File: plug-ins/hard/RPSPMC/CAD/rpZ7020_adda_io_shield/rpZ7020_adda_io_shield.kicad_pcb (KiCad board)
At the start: 4 copper layers, 61.3 x 89.9 mm, 24 parts, among them J1 Samtec_ASP-134486-01, J2-FMC-RP1 Conn_02x20, J3-FMC-POWER1 Conn_02x06_Odd_Even, J4-FMC-AUX1 Conn_02x06_Odd_Even

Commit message: fine tune brd
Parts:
- moved MH0 0.51 mm to (122.1, 159.0)
- moved MH1 0.51 mm to (175.7, 159.0)
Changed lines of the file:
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@@
 	(footprint "MountingHole:MountingHole_3.2mm_M3"
 		(layer "F.Cu")
-		(at 175.6614 158.511)
+		(at 175.6614 159.019)
 		(descr "Mounting Hole 3.2mm, no annular, M3")
 		(tags "mounting hole 3.2mm no annular m3")
@@
 	(footprint "MountingHole:MountingHole_3.2mm_M3"
 		(layer "F.Cu")
-		(at 122.0928 158.511)
+		(at 122.0928 159.019)
 		(descr "Mounting Hole 3.2mm, no annular, M3")
 		(tags "mounting hole 3.2mm no annular m3")
@@
 		(polygon
 			(pts
-				(xy 118.359 74.945) (xy 179.319 74.945) (xy 179.319 164.861) (xy 118.613 165.115)
+				(xy 118.105 74.945) (xy 179.065 74.945) (xy 179.573 164.861) (xy 118.359 164.861)
 			)
 		)

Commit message: cleanups, updated test bed code to work with new mod conf
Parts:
- added E1: Conn_02x13_Odd_Even, Connector_PinHeader_2.54mm:PinHeader_2x13_P2.54mm_Vertical, B.Cu at (124.5, 83.8)
- added E1: Conn_02x13_Odd_Even, Connector_PinHeader_2.54mm:PinHeader_2x13_P2.54mm_Vertical, B.Cu at (175.4, 83.8)
- C1, C2, C3, C4, C5, C6: footprint Capacitor_THT:C_Rect_L4.6mm_W2.0mm_P2.50mm_MKS02_FKP02 -> Capacitor_SMD:C_1206_3216Metric_Pad1.33x1.80mm_HandSolder
- moved C2 1.20 mm to (140.6, 93.9)
- moved C3 1.20 mm to (140.6, 107.4)
- moved C4 1.20 mm to (166.1, 107.4)
- moved C5 1.20 mm to (166.1, 93.9)
- moved E2 0.17 mm to (172.9, 83.8)

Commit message: work ok hat
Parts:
- removed the E1 at (124.5, 83.8)
- removed the E1 at (175.4, 83.8)
- removed MH0: MountingHole_3.2mm_M3, MountingHole:MountingHole_3.2mm_M3
- added MH2: MountingHole_3.2mm_M3, MountingHole:MountingHole_3.2mm_M3, F.Cu at (148.4, 163.0)
- added MH3: MountingHole_3.2mm_M3, MountingHole:MountingHole_3.2mm_M3, F.Cu at (180.7, 150.2)
- added MH4: MountingHole_3.2mm_M3, MountingHole:MountingHole_3.2mm_M3, F.Cu at (180.7, 77.6)
- added MH6: MountingHole_3.2mm_M3, MountingHole:MountingHole_3.2mm_M3, F.Cu at (117.4, 77.5)
- added TP-CLK: TestPoint, Connector_Pin:Pin_D0.7mm_L6.5mm_W1.8mm_FlatFork, F.Cu at (156.2, 79.0)
- added TP-GND: TestPoint, Connector_Pin:Pin_D0.7mm_L6.5mm_W1.8mm_FlatFork, F.Cu at (163.3, 76.3)
- added TP-SYNC: TestPoint, Connector_Pin:Pin_D0.7mm_L6.5mm_W1.8mm_FlatFork, F.Cu at (149.2, 79.0)
- moved MH1 59.0 mm to (117.3, 150.2)
- moved MH5 1.03 mm to (148.9, 91.9)
- renumbered J2-FMC-RP1 to J2-FMC-RP, J3-FMC-POWER1 to J3-FMC-POWER, J4-FMC-AUX1 to J4-FMC-AUX, JP-EXT-3.3V-RP1 to JP-EXT-3.3V-RP, MH3 to MH5, JPMD1 to PMD1, JPMD2 to PMD2, JPMD3 to PMD3, JPMD4 to PMD4, JPMD5 to PMD5, JPMD6 to PMD6
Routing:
- net D2P RP: track 86.4 -> 62.0 mm, vias 2 -> 0
- net +3.3V: track 108.0 -> 127.5 mm
- net CLK-ADC: track 44.1 -> 61.1 mm
- net SYNC PMOD: track 93.9 -> 109.5 mm
- net D5P RP: track 65.6 -> 54.7 mm
- net SDO2 FMC: track 26.9 -> 16.9 mm
- net EN: track 36.3 -> 45.2 mm
- net D3P RP: track 55.3 -> 46.4 mm, vias 1 -> 0
- net CNV FMC: track 26.2 -> 34.9 mm
- net SCLK PMOD: track 104.8 -> 113.2 mm
- net SCK FMC: track 31.9 -> 40.2 mm
- net SDO5 FMC: track 24.0 -> 17.1 mm
- net SDO1 FMC: track 18.2 -> 25.1 mm
- net SDO0 FMC: track 19.3 -> 25.6 mm, vias 0 -> 1
- net VADJ: track 41.4 -> 35.3 mm
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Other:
- board outline removed

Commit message: finialy Rev1.0.0, in production.
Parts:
- added J2: Conn_01x03_Socket, Connector_PinSocket_2.54mm:PinSocket_1x03_P2.54mm_Vertical, F.Cu at (117.3, 126.7)
- moved C1 1.20 mm to (140.6, 79.6)
- moved C6 1.20 mm to (166.1, 79.8)
- renumbered J2-FMC-RP to J2-FMC-RP1, J3-FMC-POWER to J3-FMC-POWER1, J4-FMC-AUX to J4-FMC-AUX1, JP-EXT-3.3V-RP to JP-EXT-3.3V-RP1, TP-GND to TP-GND1
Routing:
- net EXT 3.3V DAC: track 34.5 -> 48.8 mm
- net GND: track 529.2 -> 516.7 mm
- net D3P RP: track 46.4 -> 56.0 mm, vias 0 -> 1
- net D4P RP: track 52.8 -> 48.9 mm, vias 1 -> 0
- net D2P RP: track 62.0 -> 65.5 mm
- net D0P RP: track 21.8 -> 25.3 mm
- net I2C SCL RP: track 68.6 -> 65.7 mm
- net +3.3V: track 127.5 -> 125.4 mm
- net +12V FMC: track 28.8 -> 30.7 mm
- net SCLK PMOD: track 113.2 -> 111.7 mm
- net D5P RP: track 54.7 -> 53.4 mm, vias 1 -> 0
- net RP 3.3V: track 88.6 -> 89.4 mm
- net D1P RP: track 29.7 -> 29.0 mm, vias 1 -> 0
- net SDI3 PMOD: track 39.0 -> 38.4 mm
- net SDI5 PMOD: track 42.3 -> 41.8 mm
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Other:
- board outline added: 70.6 x 94.5 mm
- board text added: "1"
- board text added: "2"
- board text added: "3"
- board text added: "3.3E"
- board text added: "4"
- board text added: "5"
- board text added: "5V Reg"
- board text added: "6"
- board text added: "DIO0"
- board text added: "DIO1"
- board text added: "DIO2"
- board text added: "DIO3"
- board text added: "DIO4"
- board text added: "DIO5"
- board text added: "DIO6"
- board text added: "DIO7"
- board text added: "DION"
- board text added: "DIOP"
- board text added: "I2C"
- board text added: "RPSPMC Rev 1.0.0 (GPL) PyZahl-Gxsm4 BNL2025"
- board text added: "RPSPMC hat for GXSM4"
- board text added: "S"
- board text added: "Vpp"
- board text added: "https://github.com/pyzahl/Gxsm4"
- board text removed: "DAC"
- board text removed: "RPSPMC V1.0.0 (C) PyZ-Gxsm4 2025"

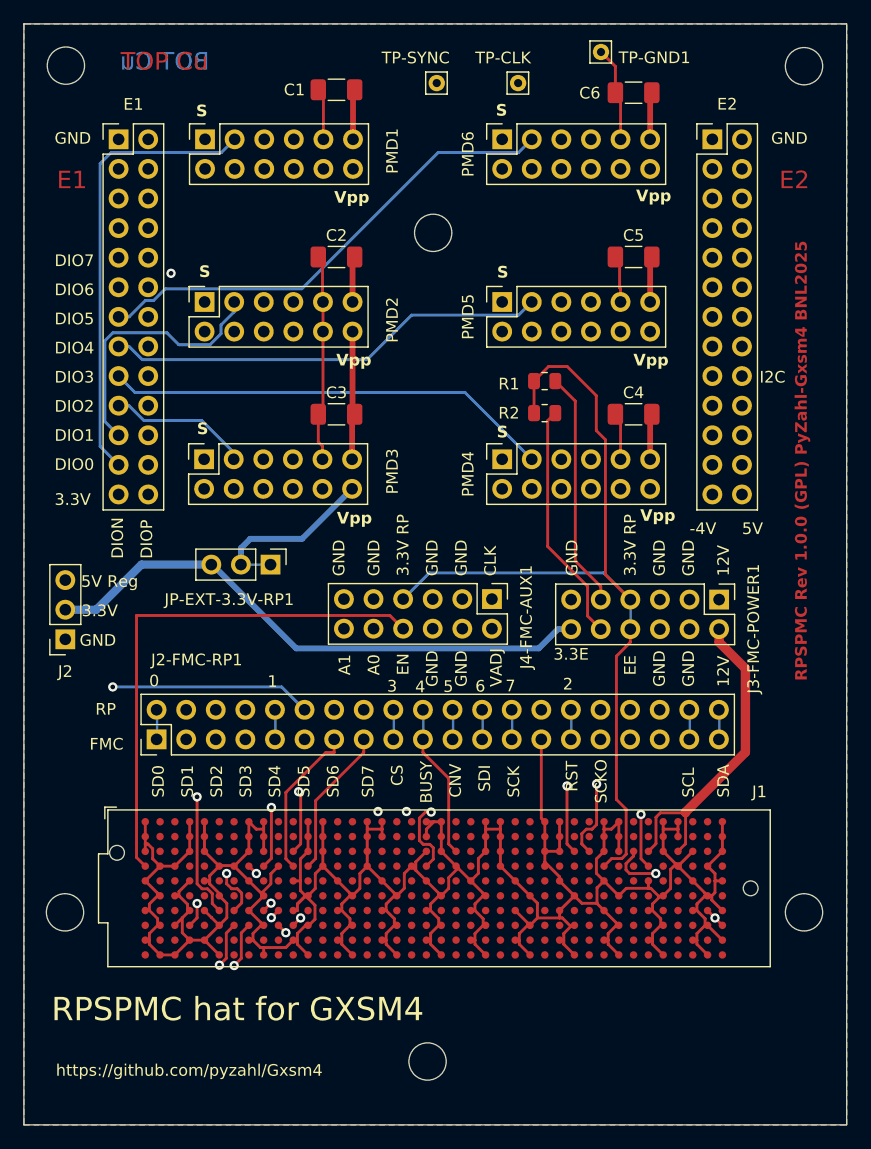
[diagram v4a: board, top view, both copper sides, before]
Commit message: patch to PCB, PMOD connector mirror issue, but no issue, easy fix. completed AD463x SPI IP -- to be tested and integarted into signals, added selector added Z-polarity switch
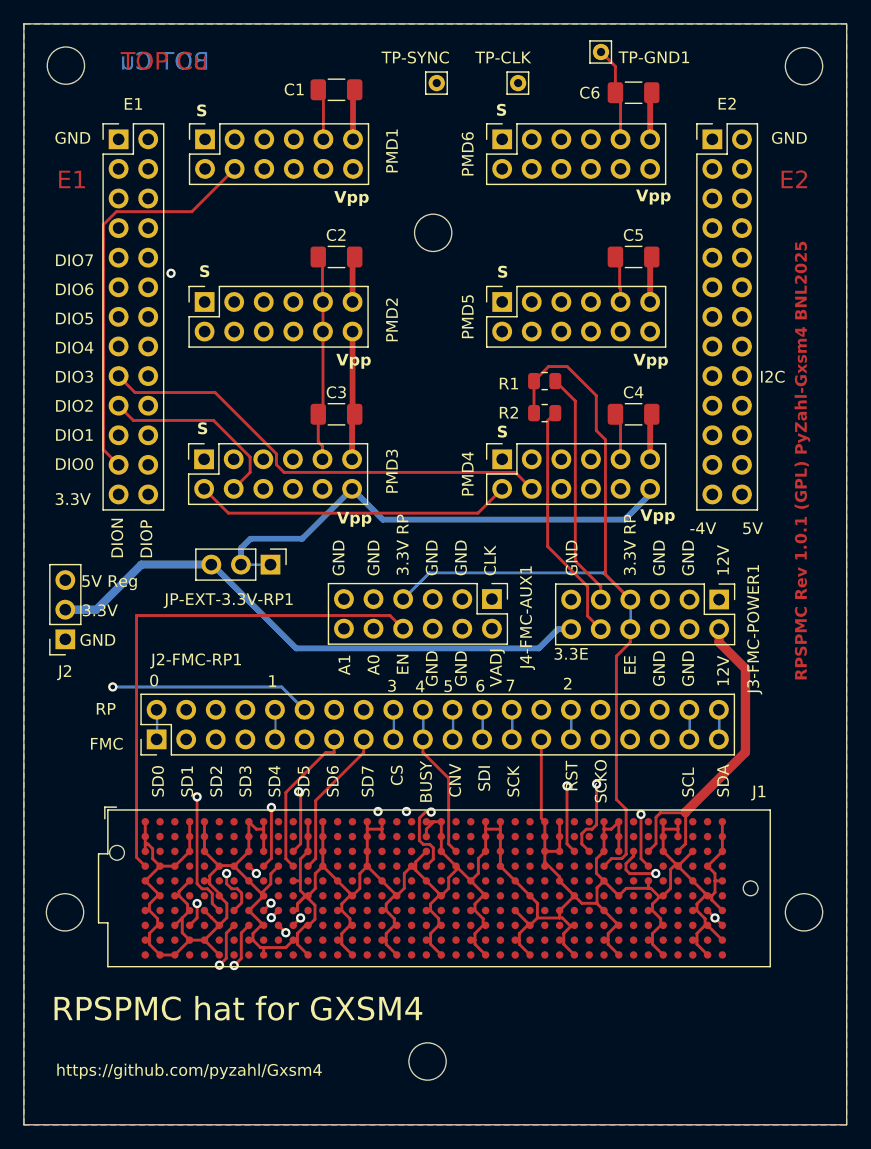
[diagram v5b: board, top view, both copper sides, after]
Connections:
- PMD1 pad 1: SYNC PMOD -> unconnected-(PMD1-Pin_1-Pad1)
- PMD1 pad 2: unconnected-(PMD1-Pin_2-Pad2) -> SYNC PMOD
- PMD1 pad 3: SDI0 PMOD -> unconnected-(PMD1-Pin_3-Pad3)
- PMD1 pad 4: unconnected-(PMD1-Pin_4-Pad4) -> SDI0 PMOD
- PMD1 pad 5: SDO0 PMOD -> unconnected-(PMD1-Pin_5-Pad5)
- PMD1 pad 6: unconnected-(PMD1-Pin_6-Pad6) -> SDO0 PMOD
- PMD1 pad 7: SCLK PMOD -> unconnected-(PMD1-Pin_7-Pad7)
- PMD1 pad 8: unconnected-(PMD1-Pin_8-Pad8) -> SCLK PMOD
- PMD2 pad 1: SYNC PMOD -> unconnected-(PMD2-Pin_1-Pad1)
- PMD2 pad 2: unconnected-(PMD2-Pin_2-Pad2) -> SYNC PMOD
- PMD2 pad 3: SDI1 PMOD -> unconnected-(PMD2-Pin_3-Pad3)
- PMD2 pad 4: unconnected-(PMD2-Pin_4-Pad4) -> SDI1 PMOD
- PMD2 pad 5: SDO1 PMOD -> unconnected-(PMD2-Pin_5-Pad5)
- PMD2 pad 6: unconnected-(PMD2-Pin_6-Pad6) -> SDO1 PMOD
- PMD2 pad 7: SCLK PMOD -> unconnected-(PMD2-Pin_7-Pad7)
- PMD2 pad 8: unconnected-(PMD2-Pin_8-Pad8) -> SCLK PMOD
- PMD3 pad 1: SYNC PMOD -> unconnected-(PMD3-Pin_1-Pad1)
- PMD3 pad 2: unconnected-(PMD3-Pin_2-Pad2) -> SYNC PMOD
- PMD3 pad 3: SDI2 PMOD -> unconnected-(PMD3-Pin_3-Pad3)
- PMD3 pad 4: unconnected-(PMD3-Pin_4-Pad4) -> SDI2 PMOD
- PMD3 pad 5: SDO2 PMOD -> unconnected-(PMD3-Pin_5-Pad5)
- PMD3 pad 6: unconnected-(PMD3-Pin_6-Pad6) -> SDO2 PMOD
- PMD3 pad 7: SCLK PMOD -> unconnected-(PMD3-Pin_7-Pad7)
- PMD3 pad 8: unconnected-(PMD3-Pin_8-Pad8) -> SCLK PMOD
- PMD4 pad 1: SYNC PMOD -> unconnected-(PMD4-Pin_1-Pad1)
- PMD4 pad 2: unconnected-(PMD4-Pin_2-Pad2) -> SYNC PMOD
- PMD4 pad 3: SDI3 PMOD -> unconnected-(PMD4-Pin_3-Pad3)
- PMD4 pad 4: unconnected-(PMD4-Pin_4-Pad4) -> SDI3 PMOD
- PMD4 pad 5: SDO3 PMOD -> unconnected-(PMD4-Pin_5-Pad5)
- PMD4 pad 6: unconnected-(PMD4-Pin_6-Pad6) -> SDO3 PMOD
- PMD4 pad 7: SCLK PMOD -> unconnected-(PMD4-Pin_7-Pad7)
- PMD4 pad 8: unconnected-(PMD4-Pin_8-Pad8) -> SCLK PMOD
- PMD5 pad 1: SYNC PMOD -> unconnected-(PMD5-Pin_1-Pad1)
- PMD5 pad 2: unconnected-(PMD5-Pin_2-Pad2) -> SYNC PMOD
- PMD5 pad 3: SDI4 PMOD -> unconnected-(PMD5-Pin_3-Pad3)
- PMD5 pad 4: unconnected-(PMD5-Pin_4-Pad4) -> SDI4 PMOD
- PMD5 pad 5: SDO4 PMOD -> unconnected-(PMD5-Pin_5-Pad5)
- PMD5 pad 6: unconnected-(PMD5-Pin_6-Pad6) -> SDO4 PMOD
- PMD5 pad 7: SCLK PMOD -> unconnected-(PMD5-Pin_7-Pad7)
- PMD5 pad 8: unconnected-(PMD5-Pin_8-Pad8) -> SCLK PMOD
- PMD6 pad 1: SYNC PMOD -> unconnected-(PMD6-Pin_1-Pad1)
- PMD6 pad 2: unconnected-(PMD6-Pin_2-Pad2) -> SYNC PMOD
- PMD6 pad 3: SDI5 PMOD -> unconnected-(PMD6-Pin_3-Pad3)
- PMD6 pad 4: unconnected-(PMD6-Pin_4-Pad4) -> SDI5 PMOD
- PMD6 pad 5: SDO5 PMOD -> unconnected-(PMD6-Pin_5-Pad5)
- PMD6 pad 6: unconnected-(PMD6-Pin_6-Pad6) -> SDO5 PMOD
- PMD6 pad 7: SCLK PMOD -> unconnected-(PMD6-Pin_7-Pad7)
- PMD6 pad 8: unconnected-(PMD6-Pin_8-Pad8) -> SCLK PMOD
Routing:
- net SCLK PMOD: track 111.7 -> 120.9 mm
- net SDI1 PMOD: track 22.9 -> 14.3 mm
- net GND: track 516.7 -> 521.8 mm
- net SDI0 PMOD: track 38.9 -> 34.4 mm
- net SDI2 PMOD: track 12.1 -> 16.4 mm
- net SDI5 PMOD: track 41.8 -> 44.5 mm
- net +3.3V: track 125.4 -> 128.1 mm
- net SYNC PMOD: track 109.6 -> 111.8 mm
- net SDI4 PMOD: track 38.0 -> 40.0 mm
- net SDI3 PMOD: track 38.4 -> 40.0 mm
- net RP 3.3V: track 89.4 -> 90.1 mm
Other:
- board text added: "RPSPMC Rev 1.0.1 (GPL) PyZahl-Gxsm4 BNL2025"
- board text removed: "RPSPMC Rev 1.0.0 (GPL) PyZahl-Gxsm4 BNL2025"

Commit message: RPSPMC adapter pcb updates/patches
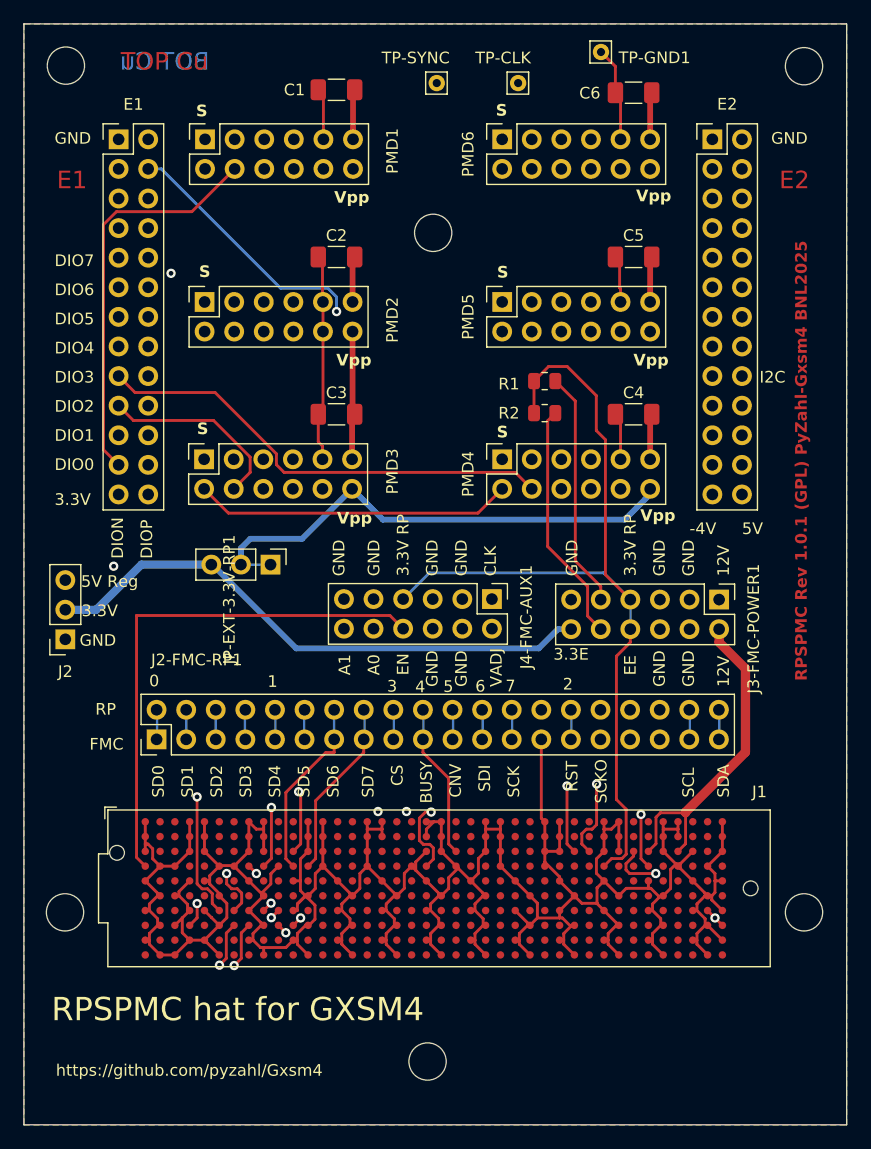
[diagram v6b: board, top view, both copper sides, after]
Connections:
- E1 pad 3: unconnected-(E1-Pin_3-Pad3) -> D10N RP
- E1 pad 4: unconnected-(E1-Pin_4-Pad4) -> D10P RP
- E1 pad 5: unconnected-(E1-Pin_5-Pad5) -> D9N RP
- E1 pad 6: unconnected-(E1-Pin_6-Pad6) -> D9P RP
- E1 pad 7: unconnected-(E1-Pin_7-Pad7) -> D8N RP
- E1 pad 8: unconnected-(E1-Pin_8-Pad8) -> D8P RP
- J2-FMC-RP1 pad 12: D3P RP -> D8P RP
- J2-FMC-RP1 pad 14: unconnected-(J2-FMC-RP1-Pin_14-Pad14) -> D9P RP
- J2-FMC-RP1 pad 16: unconnected-(J2-FMC-RP1-Pin_16-Pad16) -> D10P RP
- J2-FMC-RP1 pad 4: D2P RP -> D10N RP
- J2-FMC-RP1 pad 6: unconnected-(J2-FMC-RP1-Pin_6-Pad6) -> D9N RP
- J2-FMC-RP1 pad 8: unconnected-(J2-FMC-RP1-Pin_8-Pad8) -> D8N RP
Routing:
- net D8P RP: track 0.00 -> 62.5 mm
- net D9P RP: track 0.00 -> 62.2 mm
- net D10P RP: track 0.00 -> 59.1 mm, vias 0 -> 1
- net D10N RP: track 0.00 -> 52.0 mm
- net D9N RP: track 0.00 -> 49.9 mm
- net D8N RP: track 0.00 -> 47.4 mm
- net D3P RP: track 56.0 -> 48.1 mm
- net +3.3V: track 128.1 -> 135.0 mm
- net D2P RP: track 65.5 -> 70.0 mm

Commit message: update of rpspmc PCB
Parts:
- added J2-PWR3: Conn_01x03_Pin, Connector_JST:JST_PH_B3B-PH-K_1x03_P2.00mm_Vertical, F.Cu at (117.1, 135.8)
- added J3-PWR12: Conn_01x02_Pin, Connector_JST:JST_PH_B2B-PH-K_1x02_P2.00mm_Vertical, F.Cu at (180.0, 125.7)
- added TP-CLK1: TestPoint, Connector_Pin:Pin_D0.7mm_L6.5mm_W1.8mm_FlatFork, F.Cu at (153.3, 79.0)
- added TP-GND2: TestPoint, Connector_Pin:Pin_D0.7mm_L6.5mm_W1.8mm_FlatFork, F.Cu at (172.6, 76.5)
- added TP-SYNC1: TestPoint, Connector_Pin:Pin_D0.7mm_L6.5mm_W1.8mm_FlatFork, F.Cu at (146.4, 79.0)
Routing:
- net GND: track 521.8 -> 552.4 mm
- net 5V USB: track 0.00 -> 11.4 mm
- net EXT 3.3V DAC: track 48.8 -> 59.6 mm
- net +12V FMC: track 30.9 -> 37.6 mm
- net SCLK PMOD: track 120.9 -> 123.8 mm
- net SYNC PMOD: track 111.8 -> 114.5 mm
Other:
- board text added: "DI10"
- board text added: "DIO8"
- board text added: "DIO9"
